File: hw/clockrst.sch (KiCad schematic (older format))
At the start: 16 parts, among them SW101 SW_Push, SW102 SW_Push, SW103 SW_Push, SW104 SW_Push, SW105 SW_Push, U101 ATTINY2313-20PU, U102 ULN2803A

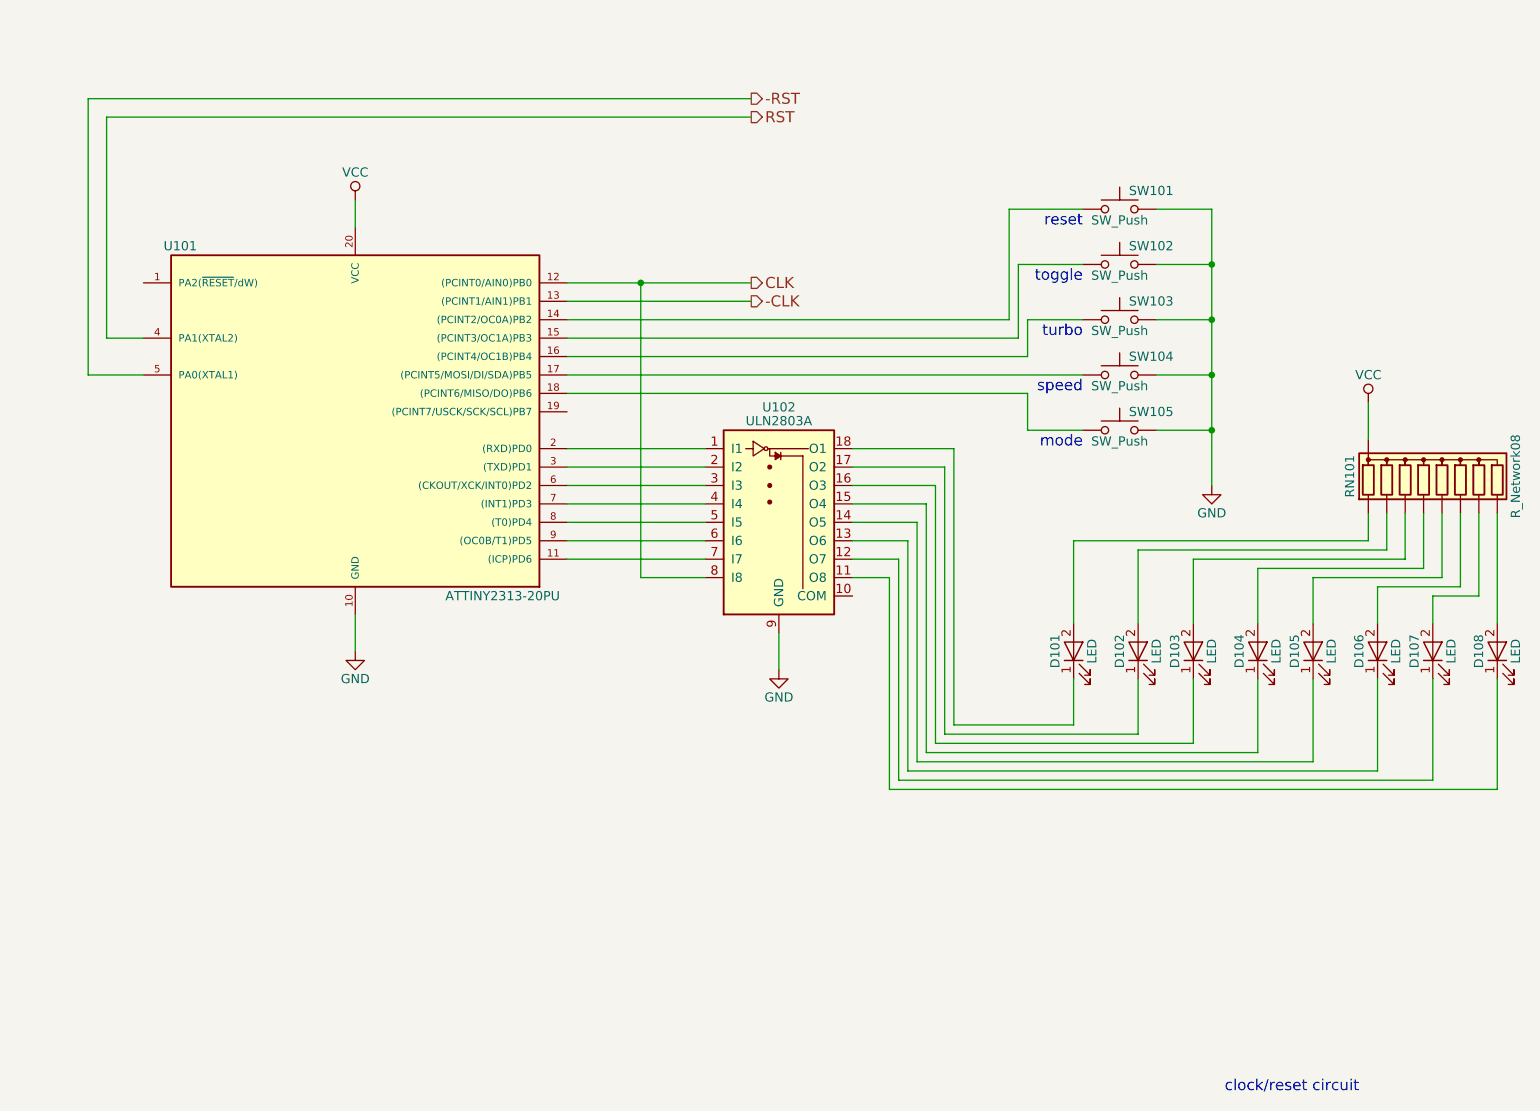
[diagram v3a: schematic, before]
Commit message: use a buffer to replicate clock/reset signals
In particular, this allows us to limit the clock fan-out
to 8 inputs.
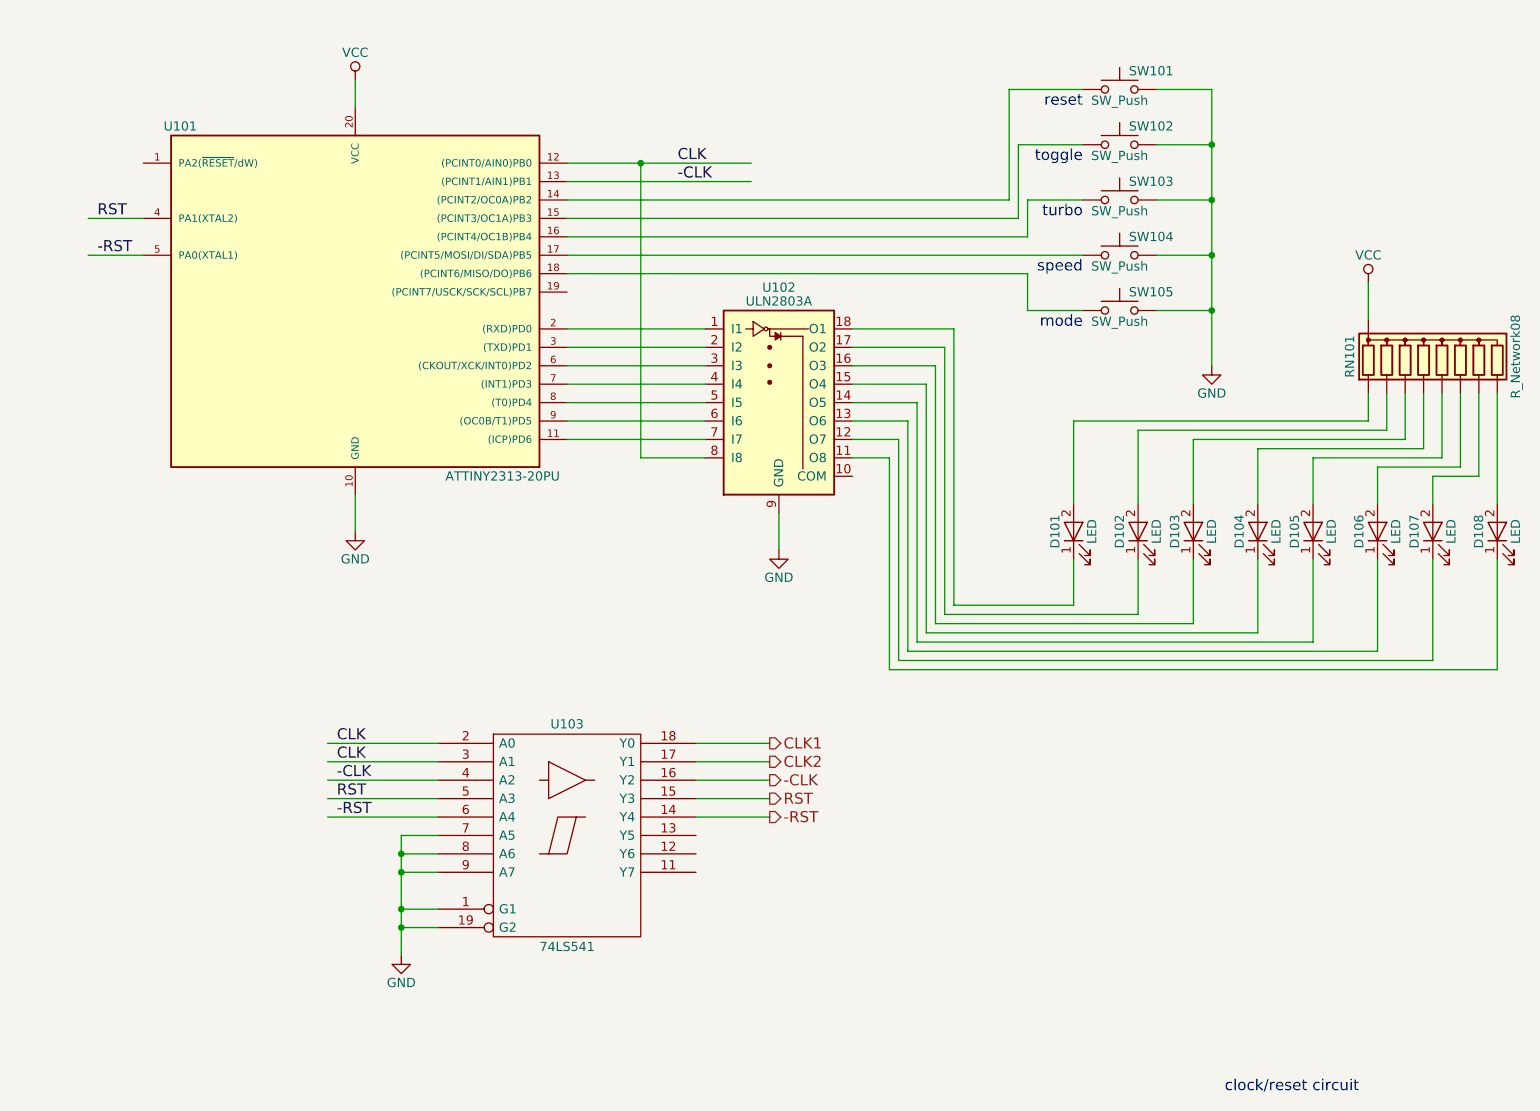
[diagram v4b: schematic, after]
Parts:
- added U103: 74LS541, symbol 74LS541
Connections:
- net labels added: CLK1, CLK2
- wire segments 94 -> 115
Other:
- moved on the sheet: D101, D102, D103, D104, D105, D106, D107, D108, RN101, SW101, SW102, SW103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

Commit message: indicate HC series part for clock/reset buffer
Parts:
- U103: value 74LS541 -> 74HC541
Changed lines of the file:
@@
 P 3700 5400
 F 0 "U103" H 3700 5975 50  0000 C BNN
-F 1 "74LS541" H 3700 4825 50  0000 C TNN
+F 1 "74HC541" H 3700 4825 50  0000 C TNN
 F 2 "" H 3700 5400 50  0001 C CNN
 F 3 "" H 3700 5400 50  0001 C CNN

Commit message: add note about protoclock firmware
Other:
- note added: "firmware is in protoclock.c"
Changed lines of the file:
@@
 Text Label 4300 1850 0    60   ~ 0
 -CLK
+Text Notes 2000 1050 0    60   ~ 0
+firmware is in protoclock.c
 $EndSCHEMATC

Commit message: buffer clock/reset signals in earlyrst module
This is the place that makes sense because the late
reset signal is the one that matters to the rest
of the circuit.
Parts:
- removed U103: 74HC541, symbol 74LS541
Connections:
- net labels removed: CLK1, CLK2
- wire segments 115 -> 94
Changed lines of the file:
@@
 Text Notes 8000 6800 2    60   ~ 0
 clock/reset circuit
-$Comp
-L 74LS541 U103
-U 1 1 595B25BA
-P 3700 5400
-F 0 "U103" H 3700 5975 50  0000 C BNN
-F 1 "74HC541" H 3700 4825 50  0000 C TNN
-F 2 "" H 3700 5400 50  0001 C CNN
-F 3 "" H 3700 5400 50  0001 C CNN
-	1    3700 5400
-	1    0    0    -1
-$EndComp
-Text Label 2450 4900 0    60   ~ 0
-CLK
-Text Label 2450 5000 0    60   ~ 0
-CLK
-Text Label 2450 5100 0    60   ~ 0
--CLK
-Text Label 2450 5200 0    60   ~ 0
-RST
-Text Label 2450 5300 0    60   ~ 0
--RST
 Wire Wire Line
 	3700 1950 6100 1950
@@
 	6900 1350 7200 1350
 Wire Wire Line
-	7200 1350 7200 1650
-Wire Wire Line
-	7200 1650 7200 1950
-Wire Wire Line
-	7200 1950 7200 2250
-Wire Wire Line
-	7200 2250 7200 2550
-Wire Wire Line
-	7200 2550 7200 2850
+	7200 1350 7200 2850
 Wire Wire Line
 	6900 1650 7200 1650
@@
 	3700 3250 4450 3250
 Wire Wire Line
-	3700 1750 4100 1750
-Wire Wire Line
-	4100 1750 4700 1750
+	3700 1750 4700 1750
 Wire Wire Line
 	4100 1750 4100 3350
@@
 	8050 2600 8050 2400
 Wire Wire Line
-	1400 2050 1100 2050
-Wire Wire Line
-	1400 2250 1100 2250
-Wire Wire Line
-	3000 4900 2400 4900
-Wire Wire Line
-	3000 5000 2400 5000
-Wire Wire Line
-	3000 5100 2400 5100
-Wire Wire Line
-	3000 5200 2400 5200
-Wire Wire Line
-	3000 5300 2400 5300
-Wire Wire Line
-	4400 4900 4800 4900
-Wire Wire Line
-	4400 5000 4800 5000
-Wire Wire Line
-	4400 5100 4800 5100
-Wire Wire Line
-	4400 5200 4800 5200
-Wire Wire Line
-	4400 5300 4800 5300
-Text HLabel 4800 4900 2    60   Output ~ 0
-CLK1
-Text HLabel 4800 5000 2    60   Output ~ 0
-CLK2
-Text HLabel 4800 5100 2    60   Output ~ 0
+	700  2050 1400 2050
+Wire Wire Line
+	800  2250 1400 2250
+Text HLabel 4700 1850 2    60   Output ~ 0
 -CLK
-Text HLabel 4800 5200 2    60   Output ~ 0
+Text HLabel 900  2600 2    60   Output ~ 0
 RST
-Text HLabel 4800 5300 2    60   Output ~ 0
+Text HLabel 900  2500 2    60   Output ~ 0
 -RST
-Wire Wire Line
-	3000 5400 2800 5400
-Wire Wire Line
-	2800 5400 2800 5500
-Wire Wire Line
-	2800 5500 2800 5600
-Wire Wire Line
-	2800 5600 2800 5800
-Wire Wire Line
-	2800 5800 2800 5900
-Wire Wire Line
-	2800 5900 2800 6050
-Wire Wire Line
-	3000 5500 2800 5500
-Connection ~ 2800 5500
-Wire Wire Line
-	3000 5600 2800 5600
-Connection ~ 2800 5600
-Wire Wire Line
-	3000 5800 2800 5800
-Connection ~ 2800 5800
-Wire Wire Line
-	3000 5900 2800 5900
-Connection ~ 2800 5900
-$Comp
-L GND #PWR?
-U 1 1 595B35FD
-P 2800 6050
-F 0 "#PWR?" H 2800 5800 50  0001 C CNN
-F 1 "GND" H 2800 5900 50  0000 C CNN
-F 2 "" H 2800 6050 50  0001 C CNN
-F 3 "" H 2800 6050 50  0001 C CNN
-	1    2800 6050
-	1    0    0    -1
-$EndComp
 Text Label 1150 2250 0    60   ~ 0
 -RST
@@
 Text Notes 2000 1050 0    60   ~ 0
 firmware is in protoclock.c
+Text HLabel 4700 1750 2    60   Output ~ 0
+CLK
+Wire Wire Line
+	800  2250 800  2500
+Wire Wire Line
+	800  2500 900  2500
+Wire Wire Line
+	700  2050 700  2600
+Wire Wire Line
+	700  2600 900  2600
 $EndSCHEMATC
